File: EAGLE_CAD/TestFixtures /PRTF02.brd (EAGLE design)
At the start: 128 x 71 mm, 41 parts

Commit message: PR9020 Gerbers
PR9020 Gerbers, organized folders
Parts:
- added U$20: PINHD-1X10, adafruit:1X10-BIG
- added U1: V_REG_317SMD, SparkFun-PowerIC:SOT223
- moved ISP1 25.9 mm to (96.7, 64.6)
- moved U$19 9.21 mm to (122.7, 62.0), turned to 270 degrees
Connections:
- new net N$1: U$19.TIP, U1.3
- new net T1: U$2.P$1, U$20.1
- new net T2: U$20.2, U$3.P$1
- net GND: now also U$19.RING; no longer U$2.P$1, U$3.P$1
- net VCC: now also U1.2
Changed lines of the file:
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@@
 <attribute name="MFG#" value="0908-1-15-20-75-14-11-0 " x="48" y="37" size="1.778" layer="27" display="off"/>
 </element>
-<element name="U$19" library="adafruit" package="PJ-102A" value="2.1MMJACKTHM" x="121.3" y="52.9"/>
-<element name="ISP1" library="adafruit" package="AVRISP" value="AVRISP-6" x="122.6" y="65"/>
+<element name="U$19" library="adafruit" package="PJ-102A" value="2.1MMJACKTHM" x="122.7" y="62" rot="R270"/>
+<element name="ISP1" library="adafruit" package="AVRISP" value="AVRISP-6" x="96.7" y="64.6"/>
+<element name="U1" library="SparkFun-PowerIC" package="SOT223" value="V_REG_317SMD" x="106.2" y="65"/>
+<element name="U$20" library="adafruit" package="1X10-BIG" value="PINHD-1X10" x="12.6" y="-3.8"/>
 </elements>
 <signals>
@@
 <contactref element="T2" pad="TP"/>
 <contactref element="T3" pad="TP"/>
-<contactref element="U$2" pad="P$1"/>
-<contactref element="U$3" pad="P$1"/>
 <contactref element="U$4" pad="P$1"/>
 <contactref element="ISP1" pad="6"/>
@@
 <vertex x="0" y="71"/>
 </polygon>
+<contactref element="U$19" pad="RING"/>
 </signal>
 <signal name="!RST">
@@
 <contactref element="U$6" pad="P$1"/>
 <contactref element="ISP1" pad="2"/>
-<wire x1="60" y1="40" x2="123.87" y2="67.54" width="0" layer="19" extent="16-16"/>
+<contactref element="U1" pad="2"/>
+<wire x1="97.97" y1="67.14" x2="106.2" y2="61.9012" width="0" layer="19" extent="1-1"/>
+<wire x1="60" y1="40" x2="97.97" y2="67.14" width="0" layer="19" extent="16-16"/>
 <wire x1="34" y1="64" x2="60" y2="40" width="0" layer="19" extent="16-16"/>
 </signal>
@@
 <contactref element="U$11" pad="P$1"/>
 <contactref element="ISP1" pad="1"/>
-<wire x1="49" y1="64" x2="121.33" y2="67.54" width="0" layer="19" extent="1-1"/>
+<wire x1="49" y1="64" x2="95.43" y2="67.14" width="0" layer="19" extent="1-1"/>
 </signal>
 <signal name="SCK">
 <contactref element="U$12" pad="P$1"/>
 <contactref element="ISP1" pad="3"/>
-<wire x1="37" y1="67" x2="121.33" y2="65" width="0" layer="19" extent="1-1"/>
+<wire x1="37" y1="67" x2="95.43" y2="64.6" width="0" layer="19" extent="1-1"/>
 </signal>
 <signal name="MOSI">
 <contactref element="U$14" pad="P$1"/>
 <contactref element="ISP1" pad="4"/>
-<wire x1="39" y1="68" x2="123.87" y2="65" width="0" layer="19" extent="1-1"/>
+<wire x1="39" y1="68" x2="97.97" y2="64.6" width="0" layer="19" extent="1-1"/>
 </signal>
 <signal name="RST">
 <contactref element="ISP1" pad="5"/>
 </signal>
+<signal name="N$1">
+<contactref element="U$19" pad="TIP"/>
+<contactref element="U1" pad="3"/>
+<wire x1="108.5114" y1="61.9012" x2="113.41" y2="61.9" width="0" layer="19" extent="1-1"/>
+</signal>
+<signal name="T2">
+<contactref element="U$3" pad="P$1"/>
+<contactref element="U$20" pad="2"/>
+<wire x1="3.71" y1="-3.8" x2="60" y2="35" width="0" layer="19" extent="1-1"/>
+</signal>
+<signal name="T1">
+<contactref element="U$2" pad="P$1"/>
+<contactref element="U$20" pad="1"/>
+<wire x1="1.17" y1="-3.8" x2="10.6" y2="44.6" width="0" layer="19" extent="1-1"/>
+</signal>
 </signals>

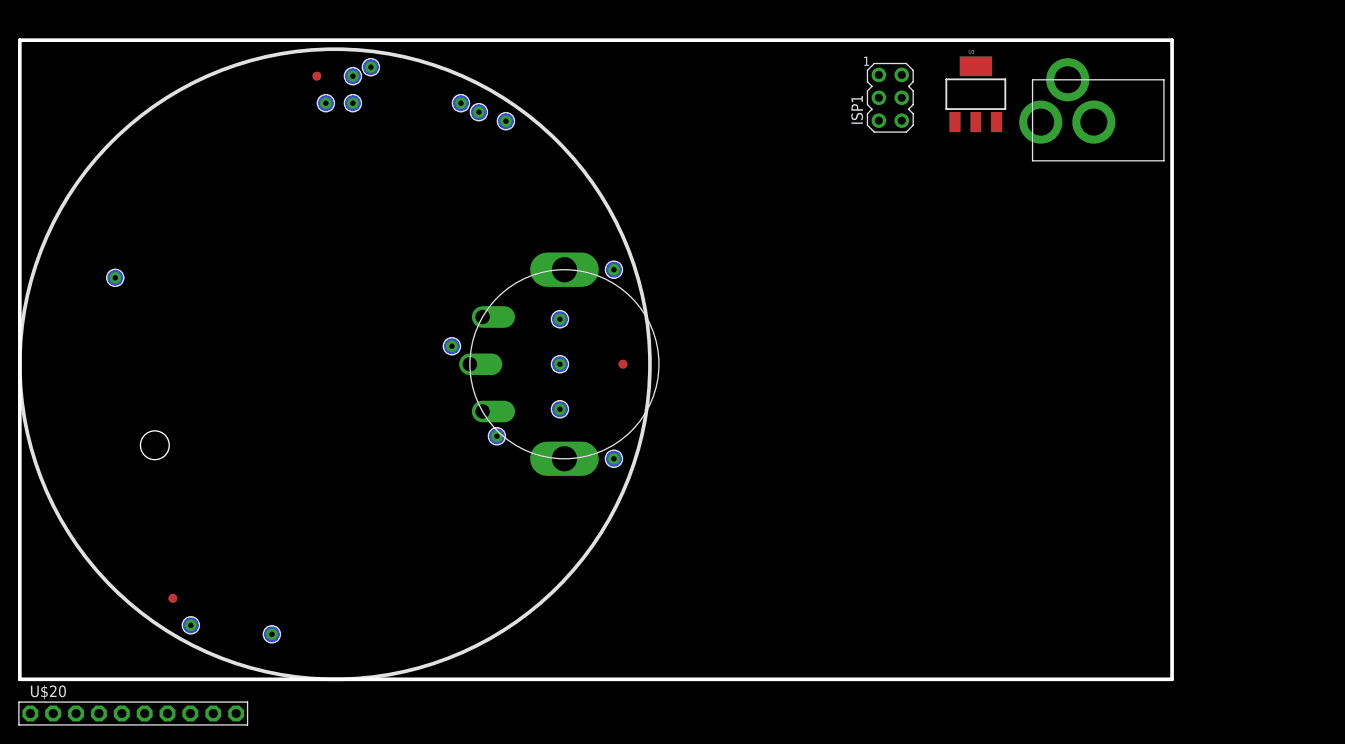
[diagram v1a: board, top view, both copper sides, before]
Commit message: Test fixture updates
Initial schematic of the test fixture for PR9020.  No real layout done.
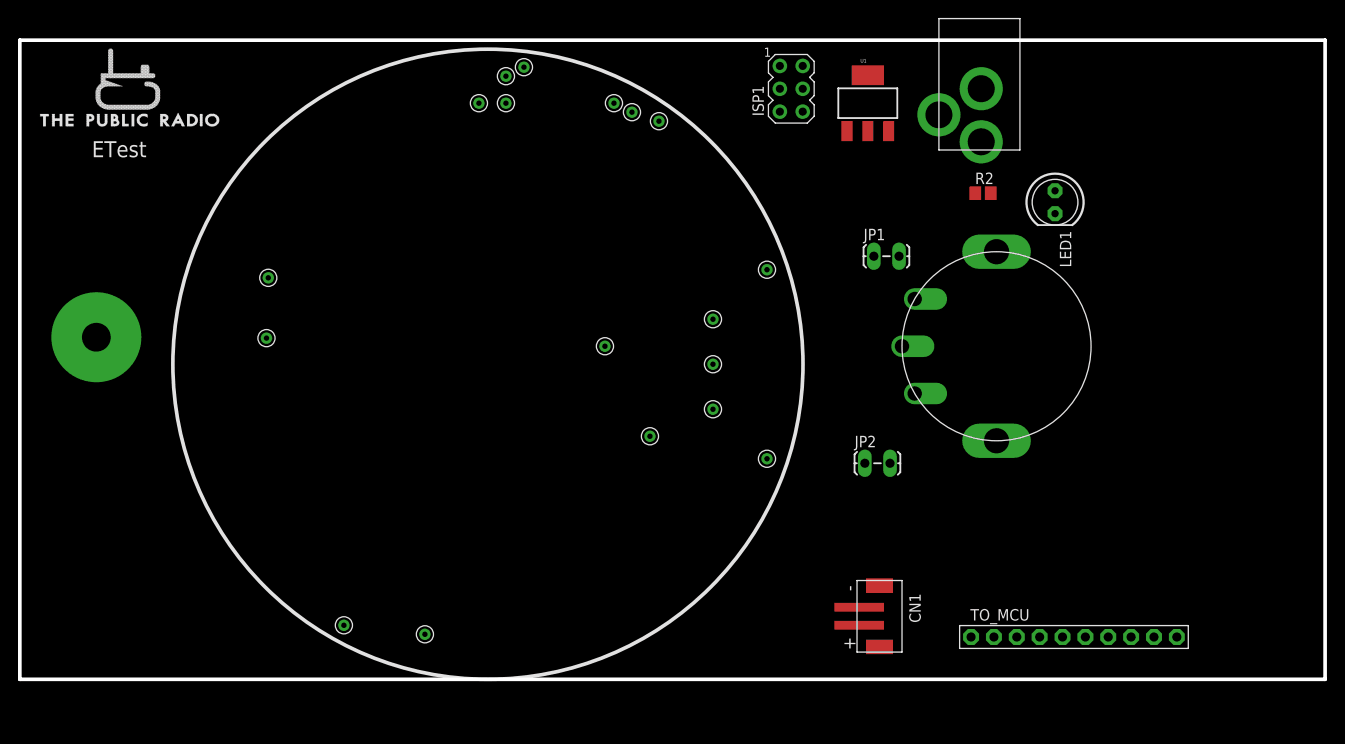
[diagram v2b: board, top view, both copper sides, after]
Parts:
- removed MARK1, MARK2, MARK3: (no value), PR_Parts_Library:FIDUCIAL_1MM
- removed T1, T10, T11, T12, T13, T14, T15, T16, T17, T2, T3, T4, T5, T6, T7, T8, T9: (no value), PR_Parts_Library:TP20R
- removed U$20: PINHD-1X10, adafruit:1X10-BIG
- added CN1: (no value), PR_Parts_Library:JST-B2B-PH-SM4-TB
- added J1: M3_SCREW_POST, PR_Parts_Library:M3_BOLT_HOLE
- added JP1, JP2: SMT/THJumper, SparkFun-Connectors:1X02_LOCK_LONGPADS
- added LED1: (no value), adafruit:LED5MM
- added R2: 1k, PR_Parts_Library:0805_ADAFRUIT
- added TO_MCU: PINHD-1X10, adafruit:1X10-BIG
- added U$21: 0908MILL_MAX_SPRINGPIN, PR_Parts_Library:0908MILL_MAX_SPRINGPIN
- moved U$1 63.8 mm to (12.0, 67.0), flipped to the top
- moved R1 48.0 mm to (108.5, 37.0)
- moved U$19 17.5 mm to (106.7, 69.0), turned to 0 degrees
- moved U$10 17.0 mm to (71.0, 62.0)
- moved U$11 17.0 mm to (66.0, 64.0)
- moved U$12 17.0 mm to (54.0, 67.0)
- moved U$13 17.0 mm to (54.0, 64.0)
- moved U$14 17.0 mm to (56.0, 68.0)
- moved U$15 17.0 mm to (83.0, 24.5)
- moved U$16 17.0 mm to (83.0, 45.5)
- moved U$17 17.0 mm to (70.0, 27.0)
- moved U$18 17.0 mm to (65.0, 37.0)
- moved U$2 17.0 mm to (27.6, 44.6)
- moved U$3 17.0 mm to (77.0, 35.0)
- moved U$4 17.0 mm to (77.0, 30.0)
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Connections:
- removed net !RST: T10.TP
- removed net A_IN: R1.SIGNAL, T16.TP, U$17.P$1
- removed net SCLK: T11.TP
- removed net SDIO: T13.TP
- removed net SW: T8.TP, U$9.P$1
- removed net T1: U$2.P$1, U$20.1
- removed net T2: U$20.2, U$3.P$1
- new net ANT: J1.P$1, U$21.P$1
- new net DUTPRES: TO_MCU.1, U$2.P$1
- new net N$2: LED1.A, R2.2
- new net N$5: JP2.1, R1.SIGNAL
- new net N$6: JP1.2, R1.WIPER
- new net N$7: JP2.2, U$17.P$1
- new net TSW: TO_MCU.4, U$9.P$1
- net A_OUT: now also JP1.1; no longer R1.WIPER, T17.TP
- net GND: now also LED1.K, U$3.P$1; no longer T1.TP, T2.TP, T3.TP
- net LED/PB4: now also R2.1; no longer T9.TP
- net RESET: no longer T12.TP
- net SPK_OUT+: now also CN1.1; no longer T6.TP
- net SPK_OUT-: now also CN1.2; no longer T7.TP
- net SW_IN: now also TO_MCU.2; no longer R1.SW_IN, T14.TP
- net SW_OUT: now also TO_MCU.3; no longer R1.SW_OUT, T15.TP
- net VCC: no longer T4.TP, T5.TP
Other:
- board size 128 x 71 mm -> 145 x 71 mm
- board text added: "ETest"
- board text removed: "PR9020 Born + tuned in Brooklyn http://thepublicrad.io"
